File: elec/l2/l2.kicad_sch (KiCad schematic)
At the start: 1 part, among them U102 DEV-15583 Teensy 4.0

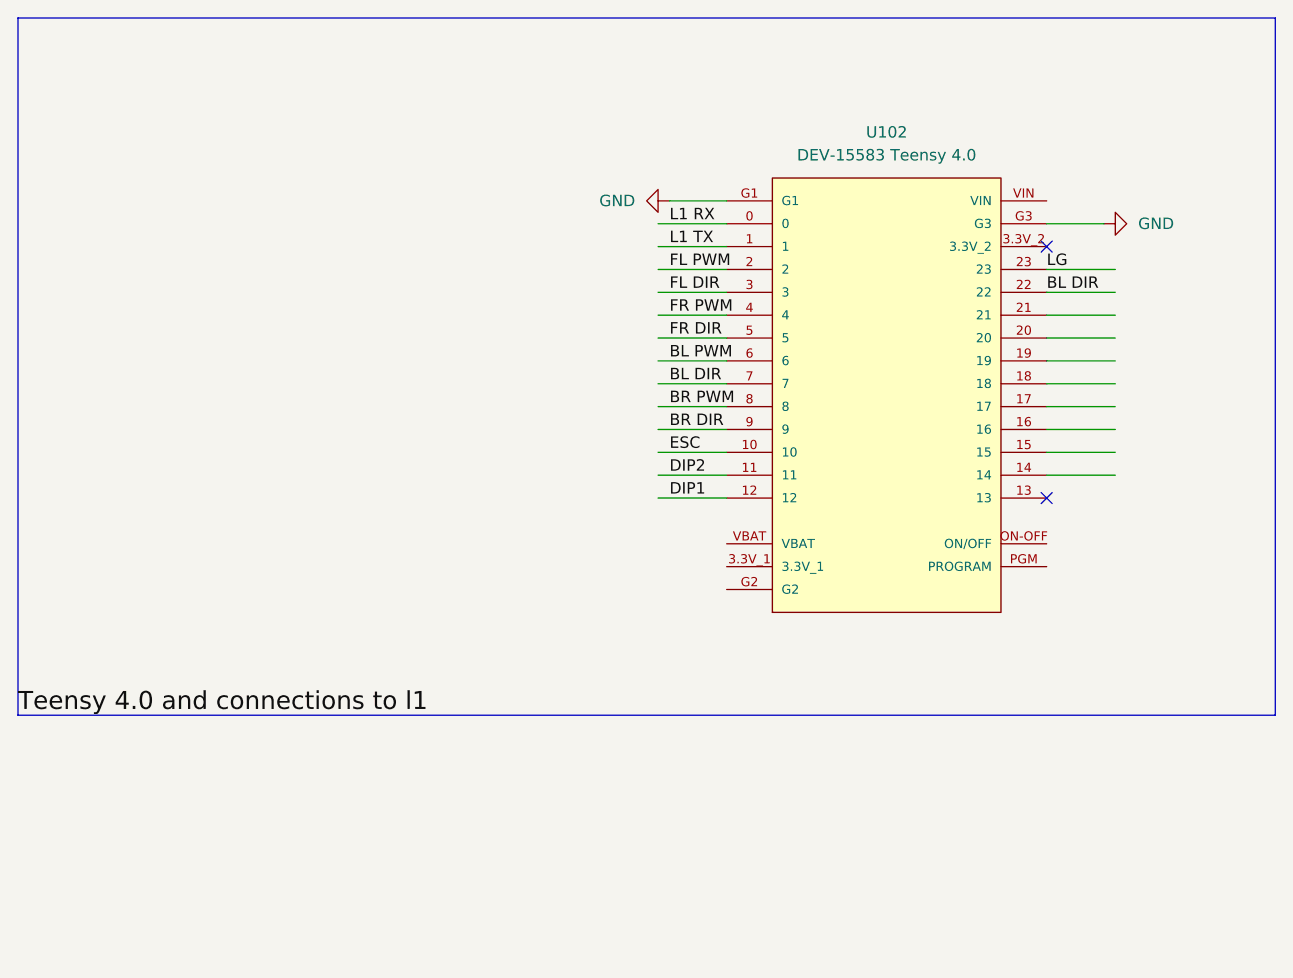
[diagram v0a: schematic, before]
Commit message: L2 net labels
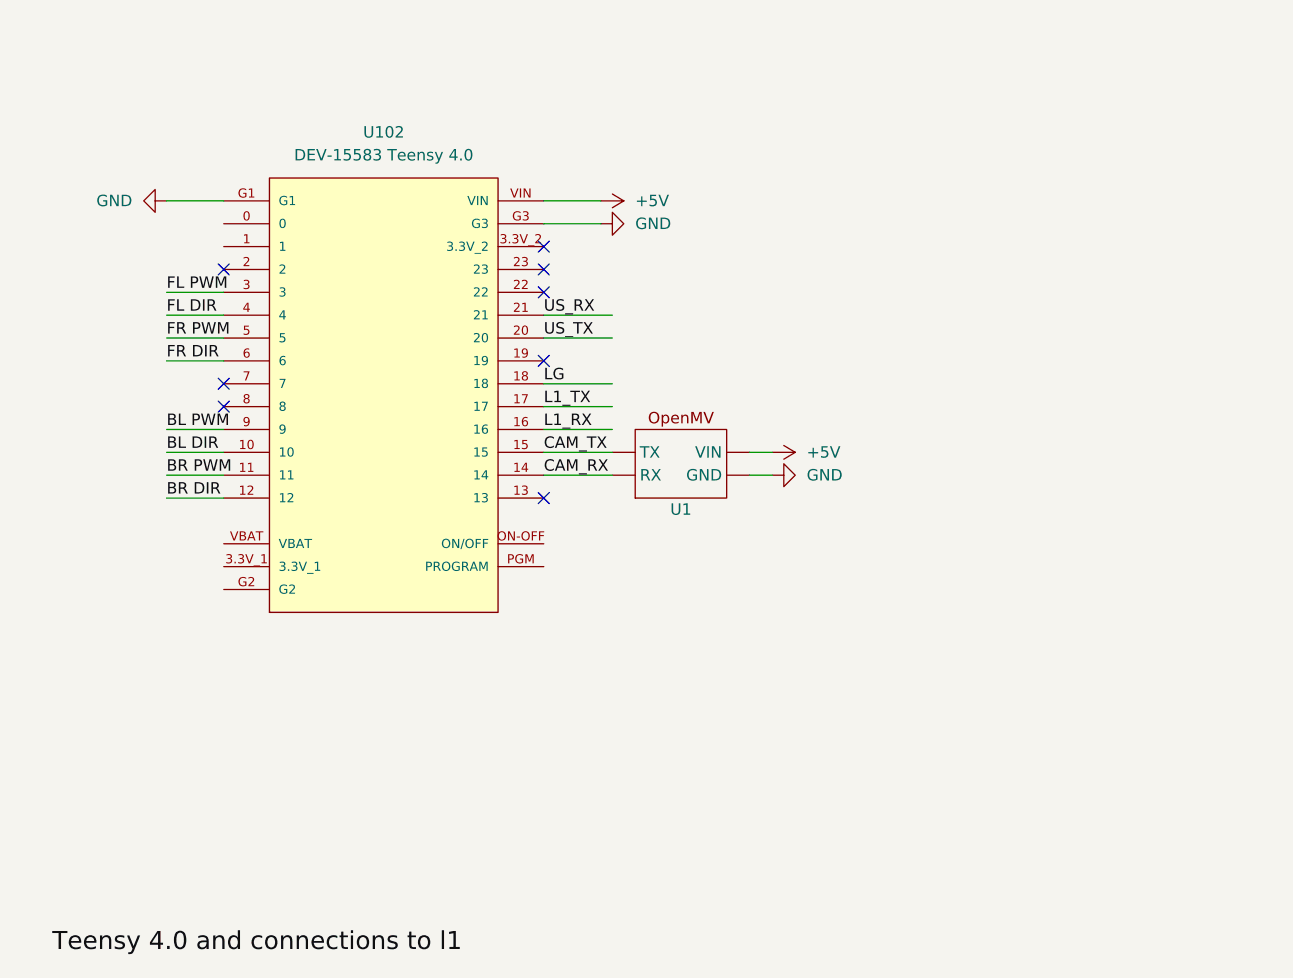
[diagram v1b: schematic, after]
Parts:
- added U1: ~, symbol openmv:OpenMV
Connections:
- net DIP1 is gone; now on net BR DIR: U102.12
- net DIP2 is gone; now on net BR PWM: U102.11
- net ESC is gone; now on net BL DIR: U102.10
- net BL DIR: no longer U102.22, U102.7
- net BL PWM: now also U102.9; no longer U102.6
- net BR DIR: no longer U102.9
- net BR PWM: no longer U102.8
- net FL DIR: now also U102.4; no longer U102.3
- net FL PWM: now also U102.3; no longer U102.2
- net FR DIR: now also U102.6; no longer U102.5
- net FR PWM: now also U102.5; no longer U102.4
- net GND: now also U1. (VIN)
- net LG: now also U102.18; no longer U102.23
- net CAM_RX: now reaches U102.14
- net CAM_RX: now also U1. (VIN)
- net CAM_TX: now reaches U102.15
- net CAM_TX: now also U1. (VIN)
- net L1_RX: now reaches U102.16
- net L1_TX: now reaches U102.17
- net US_TX: now reaches U102.20
- net US_RX: now reaches U102.21
- net +5V: now reaches U102.VIN
- net +5V: now also U1. (VIN)
- net L1 RX: no longer names the net of U102.0
- net L1 TX: no longer names the net of U102.1
- no-connect marks 2 -> 8
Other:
- moved on the sheet: U102

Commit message: Revert "L2 net labels"
This reverts commit 1f70947ea7bd54b8f040afb39f0aba0e0f35dfe9.
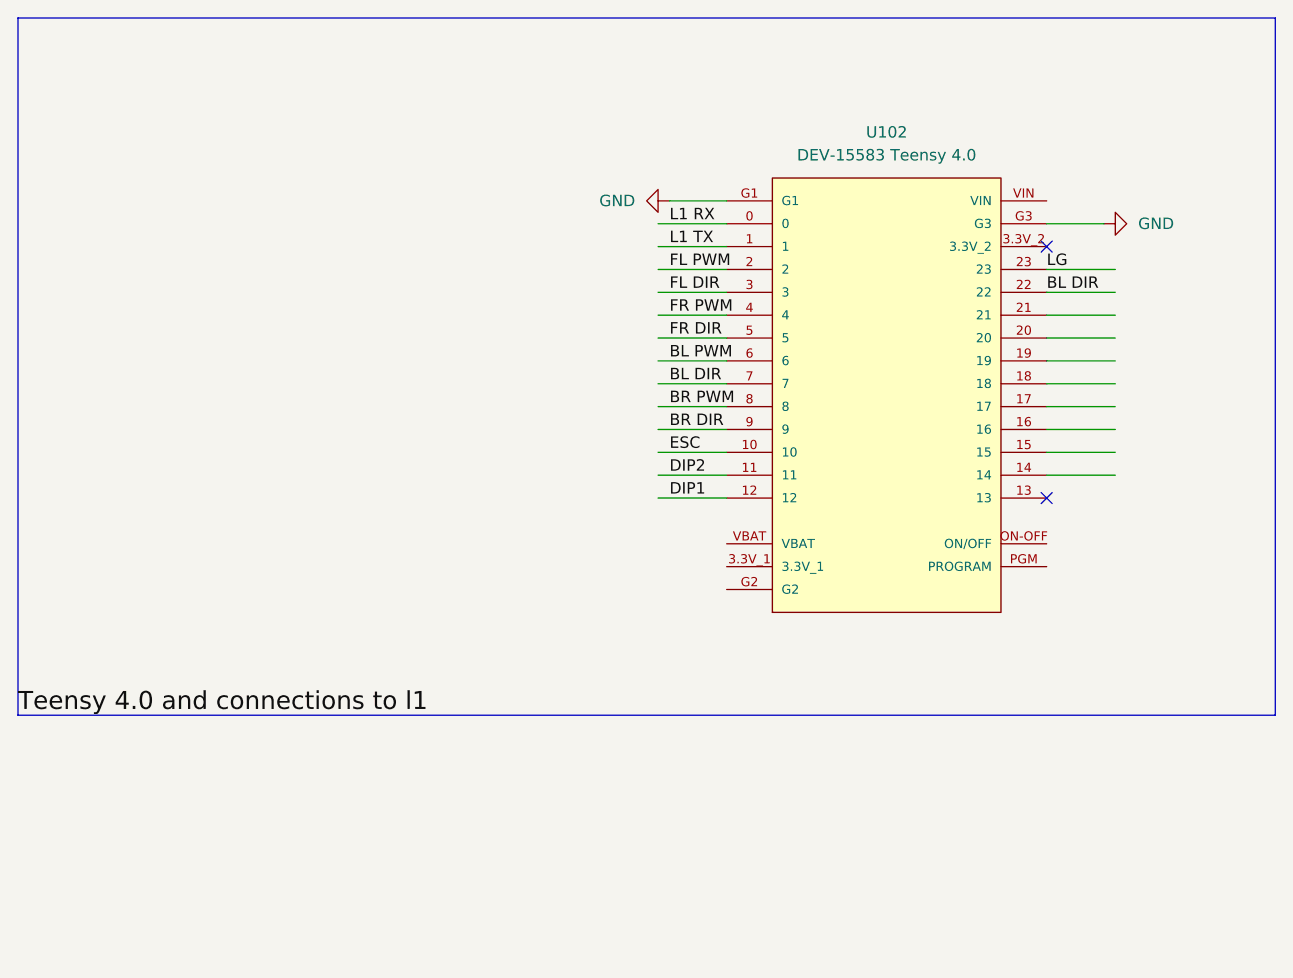
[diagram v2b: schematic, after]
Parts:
- removed U1: ~, symbol openmv:OpenMV
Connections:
- net BL DIR: now also U102.22, U102.7; no longer U102.10
- net BL PWM: now also U102.6; no longer U102.9
- net BR DIR: now also U102.9; no longer U102.12
- net BR PWM: now also U102.8; no longer U102.11
- net FL DIR: now also U102.3; no longer U102.4
- net FL PWM: now also U102.2; no longer U102.3
- net FR DIR: now also U102.5; no longer U102.6
- net FR PWM: now also U102.4; no longer U102.5
- net LG: now also U102.23; no longer U102.18
- net L1 RX: now reaches U102.0
- net L1 TX: now reaches U102.1
- net +5V: no longer names the net of U102.VIN
- net CAM_RX: no longer names the net of U102.14
- net CAM_TX: no longer names the net of U102.15
- net L1_RX: no longer names the net of U102.16
- net L1_TX: no longer names the net of U102.17
- net US_RX: no longer names the net of U102.21
- net US_TX: no longer names the net of U102.20
- new net DIP1: U102.12
- new net DIP2: U102.11
- new net ESC: U102.10
- no-connect marks 8 -> 2
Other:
- moved on the sheet: U102

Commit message: I like monkey balls.
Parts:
- added U28: xiao-esp32c3, footprints:xiao-esp32c3, symbol Seeed_Studio_XIAO_Series:xiao-esp32c3
- added U?: BNO085, footprints:bno085, symbol 4754:4754
- added U?: OpenMV H7, footprints:openmv, symbol OpenMV:OpenMV_H7
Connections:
- net BL DIR: no longer U102.22
- net GND: now also U28.12 (GND), U?.9 (GND), U?.JP1_3 (GND)
- net C TX: now reaches U102.14 (14/A0/PWM)
- net C TX: now also U?.6 (P5-UART_RX/I2C_SDA)
- net C RX: now reaches U102.15 (15/A1/PWM)
- net C RX: now also U?.5 (P4-UART_TX/I2C2_SCL)
- net SDA: now reaches U102.18 (18/A4/PWM)
- net SDA: now also U?.JP1_5 (SDA)
- net SCL: now reaches U102.19 (19/A5/PWM)
- net SCL: now also U?.JP1_4 (SCL)
- net BT TX: now reaches U102.20 (20/A6)
- net BT TX: now also U28.6 (TX)
- net BT RX: now reaches U102.21 (21/A7)
- net BT RX: now also U28.7 (RX)
- net +5V: now reaches U102.VIN
- net +5V: now also U28.13 (5V), U?.10 (VIN_(3V6-5V))
- new net +3V3: U?.JP1_1 (VIN)
- new net T_RST: U102.22 (22/A8/PWM)
- no-connect marks 2 -> 34
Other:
- moved on the sheet: U102

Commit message: trololol
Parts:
- added J1: 0526101433, footprints:522711479, symbol 52271-1479:52271-1479
- added R?: 10K, footprints:res0603, symbol Device:R
- added R?: 1K, footprints:res0603, symbol Device:R
- added SW?: SW_Push, footprints:SW_PUSH_SPST, symbol Switch:SW_Push
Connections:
- net +3V3: now also J1.1, R?.1
- net +5V: now also J1.2
- net BL DIR: now also J1.10
- net BL PWM: now also J1.9
- net BR DIR: now also J1.12
- net BR PWM: now also J1.11
- net FL DIR: now also J1.6
- net FL PWM: now also J1.5
- net FR DIR: now also J1.8
- net FR PWM: now also J1.7
- net GND: now also J1.MP1, J1.MP2, R?.2
- net L1 RX: now also J1.3
- net L1 TX: now also J1.4
- net T_RST: now also R?.2, SW?.2
- new net: R?.1, SW?.1
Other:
- moved on the sheet: U102, U28, U?

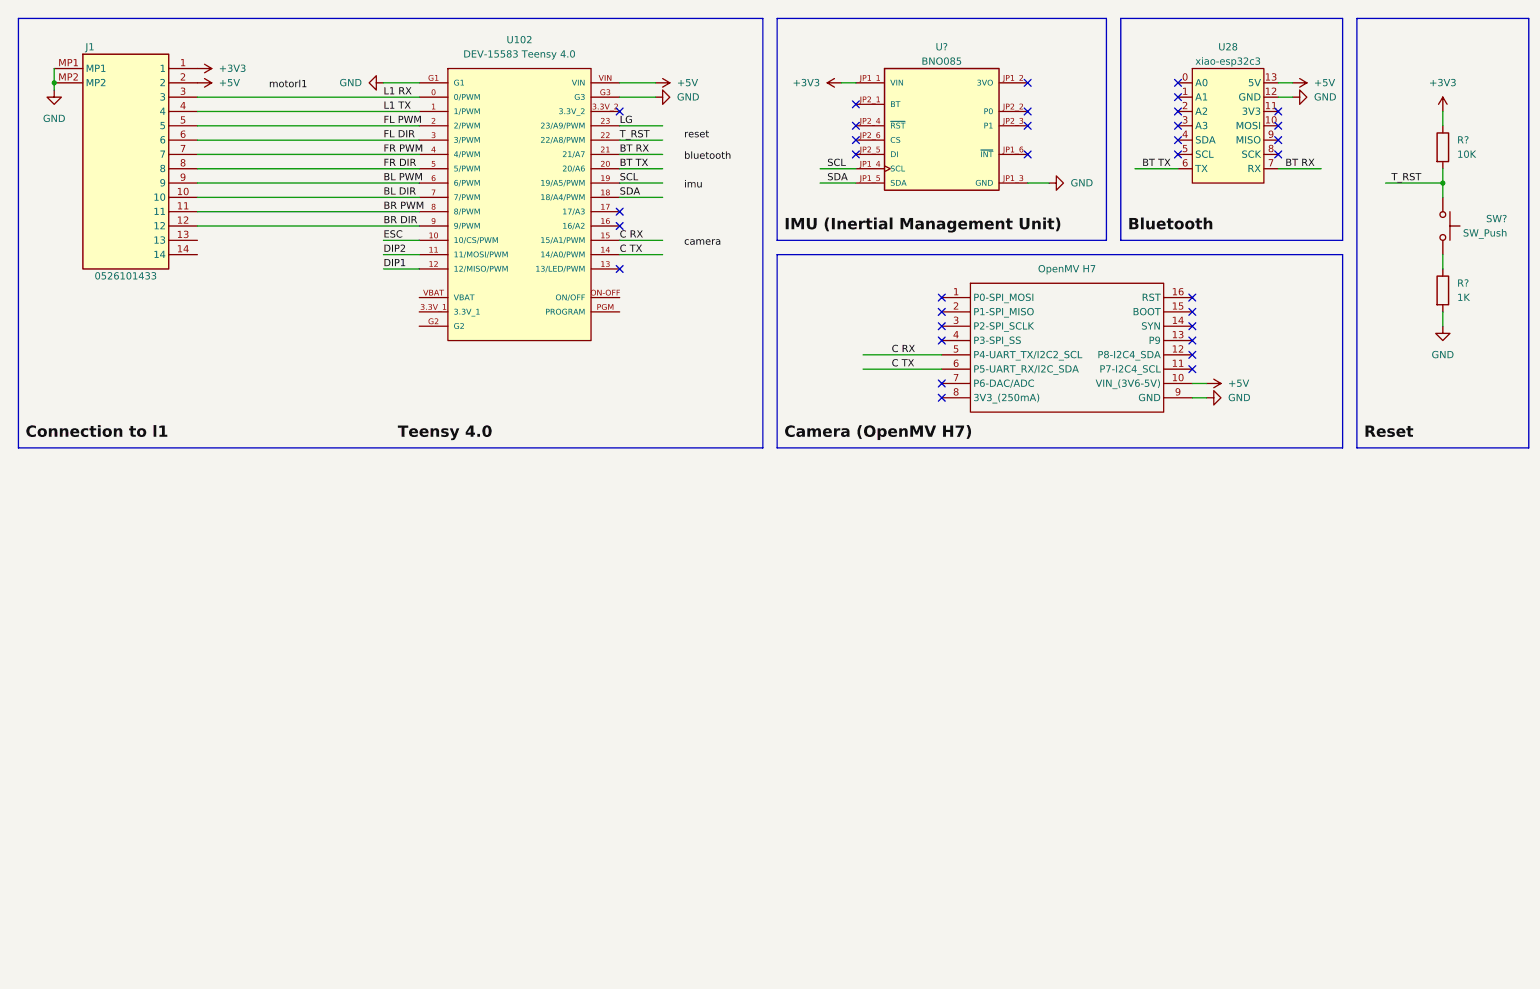
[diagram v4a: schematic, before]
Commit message: v1.0 of  L1 (sent to production), schematic for L2
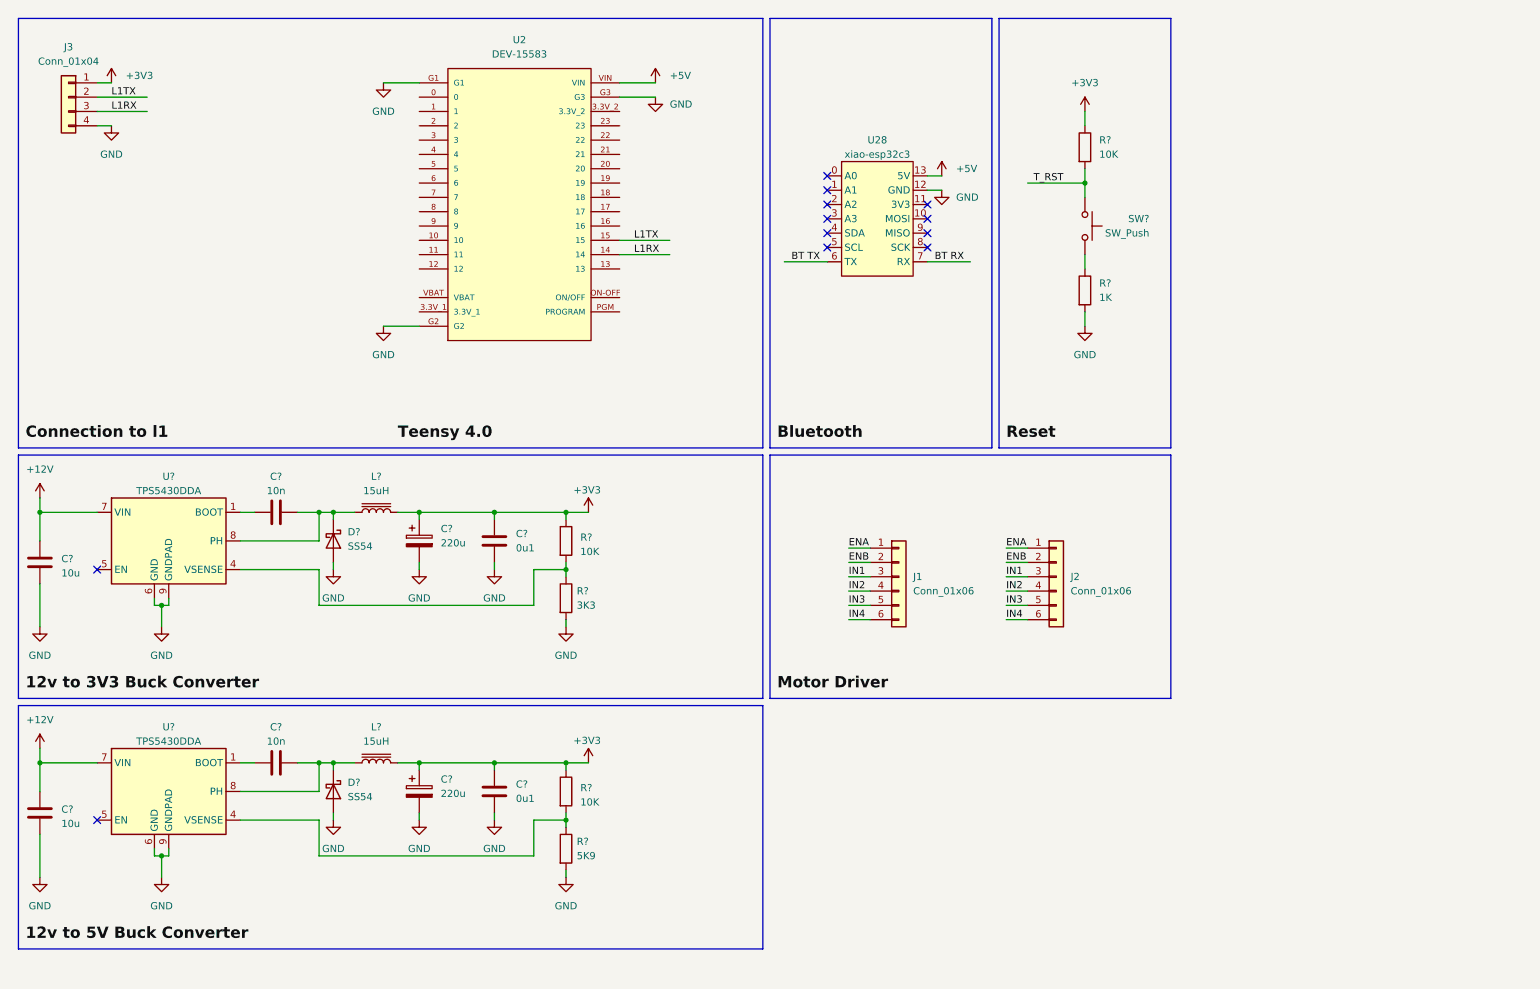
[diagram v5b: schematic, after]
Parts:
- removed J1: 0526101433, footprints:522711479, symbol 52271-1479:52271-1479
- removed U102: DEV-15583 Teensy 4.0, MODULE_DEV-15583, symbol teensy-4.0:DEV-15583
- removed U?: BNO085, footprints:bno085, symbol 4754:4754
- removed U?: OpenMV H7, footprints:openmv, symbol OpenMV:OpenMV_H7
- added C? (x2): 0u1, l2:cap0603, symbol Device:C
- added C? (x2): 10u, l2:cap0603, symbol Device:C
- added C? (x2): 220u, l2:EIA-7343-D, symbol Device:C_Polarized
- added C? (x2): 10n, l2:cap0603, symbol Device:C
- added D? (x2): SS54, l2:SMA (DO-214AC), symbol Diode:B340
- added J1, J2: Conn_01x06, Connector_PinSocket_1.00mm:PinSocket_1x06_P1.00mm_Vertical, symbol Connector_Generic:Conn_01x06
- added J3: Conn_01x04, Connector_PinSocket_1.27mm:PinSocket_1x04_P1.27mm_Vertical, symbol Connector_Generic:Conn_01x04
- added L? (x2): 15uH, l2:0630 One Piece Inductor, symbol Device:L_Iron
- added R?: 5K9, l2:res0603, symbol Device:R
- added R?: 3K3, l2:res0603, symbol Device:R
- added R? (x2): 10K, l2:res0603, symbol Device:R
- added U2: DEV-15583, DEV-15583:MODULE_DEV-15583, symbol DEV-15583:DEV-15583
- added U? (x2): TPS5430DDA, l2:TI_SO-PowerPAD-8, symbol Regulator_Switching:TPS5430DDA
- R? (x2): footprint footprints:res0603 -> l2:res0603
- SW?: footprint footprints:SW_PUSH_SPST -> l2:SW_PUSH_SPST
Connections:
- net +3V3: now also C?.1, C?.1, C?.1, C?.1, J3.1 (Pin_1), L?.2, L?.2, R?.1, R?.1
- net +5V: now also U2.VIN
- net GND: now also C?.2, C?.2, C?.2, C?.2, C?.2, C?.2, D?.2 (A), D?.2 (A), J3.4 (Pin_4), R?.2, R?.2, U2.G1, U2.G2, U2.G3, U?.6 (GND), U?.6 (GND), U?.9 (GNDPAD), U?.9 (GNDPAD)
- new net: R?.1, R?.2, U?.4 (VSENSE) (x2)
- new net: C?.2, D?.1 (K), L?.1, U?.8 (PH) (x2)
- new net: C?.1, U?.1 (BOOT) (x2)
- new net +12V: C?.1, C?.1, U?.7 (VIN), U?.7 (VIN)
- new net ENA: J1.1 (Pin_1), J2.1 (Pin_1)
- new net ENB: J1.2 (Pin_2), J2.2 (Pin_2)
- new net IN1: J1.3 (Pin_3), J2.3 (Pin_3)
- new net IN2: J1.4 (Pin_4), J2.4 (Pin_4)
- new net IN3: J1.5 (Pin_5), J2.5 (Pin_5)
- new net IN4: J1.6 (Pin_6), J2.6 (Pin_6)
- new net L1RX: J3.3 (Pin_3), U2.14
- new net L1TX: J3.2 (Pin_2), U2.15
- no-connect marks 34 -> 12
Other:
- moved on the sheet: R?, SW?, U28
